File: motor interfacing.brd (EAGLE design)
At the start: 160 x 100 mm, 14 parts

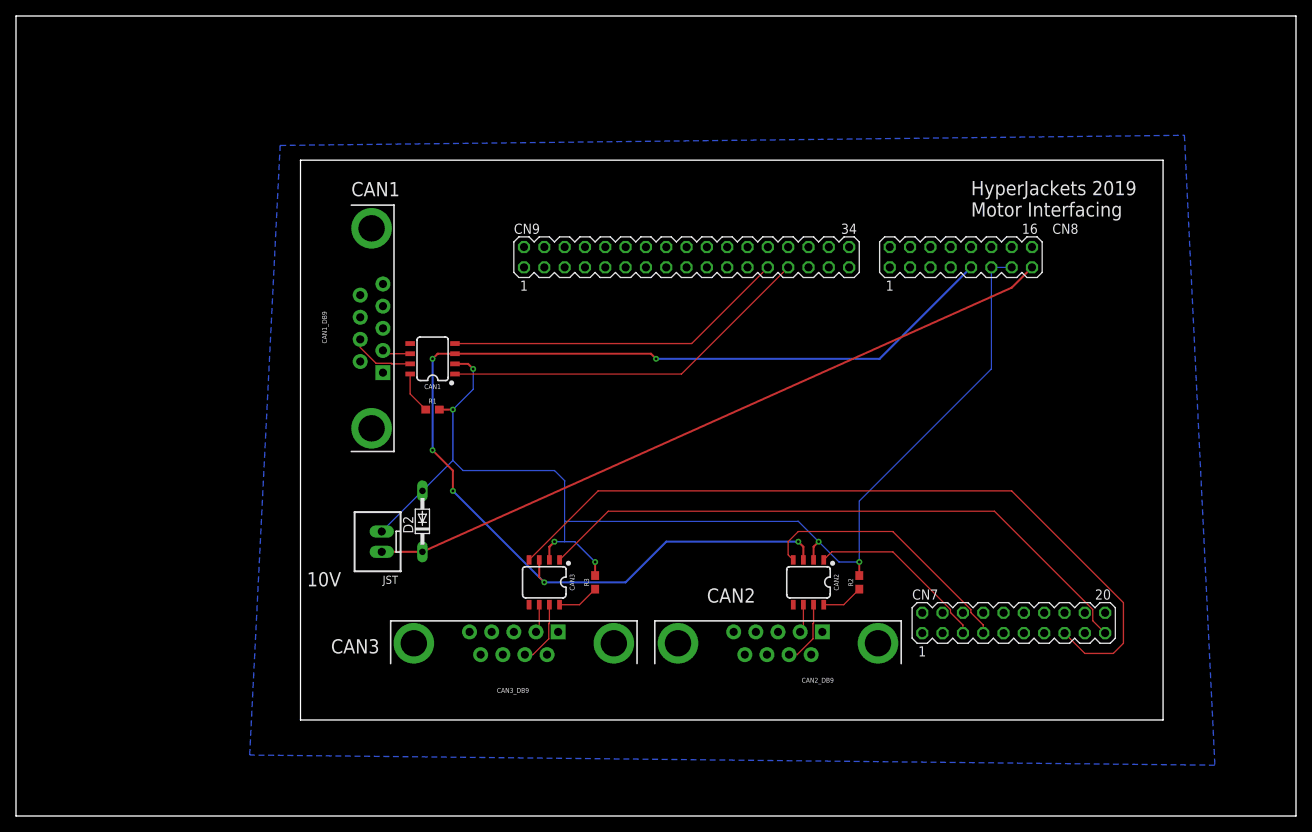
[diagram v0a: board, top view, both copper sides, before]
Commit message: Update motor interfacing board
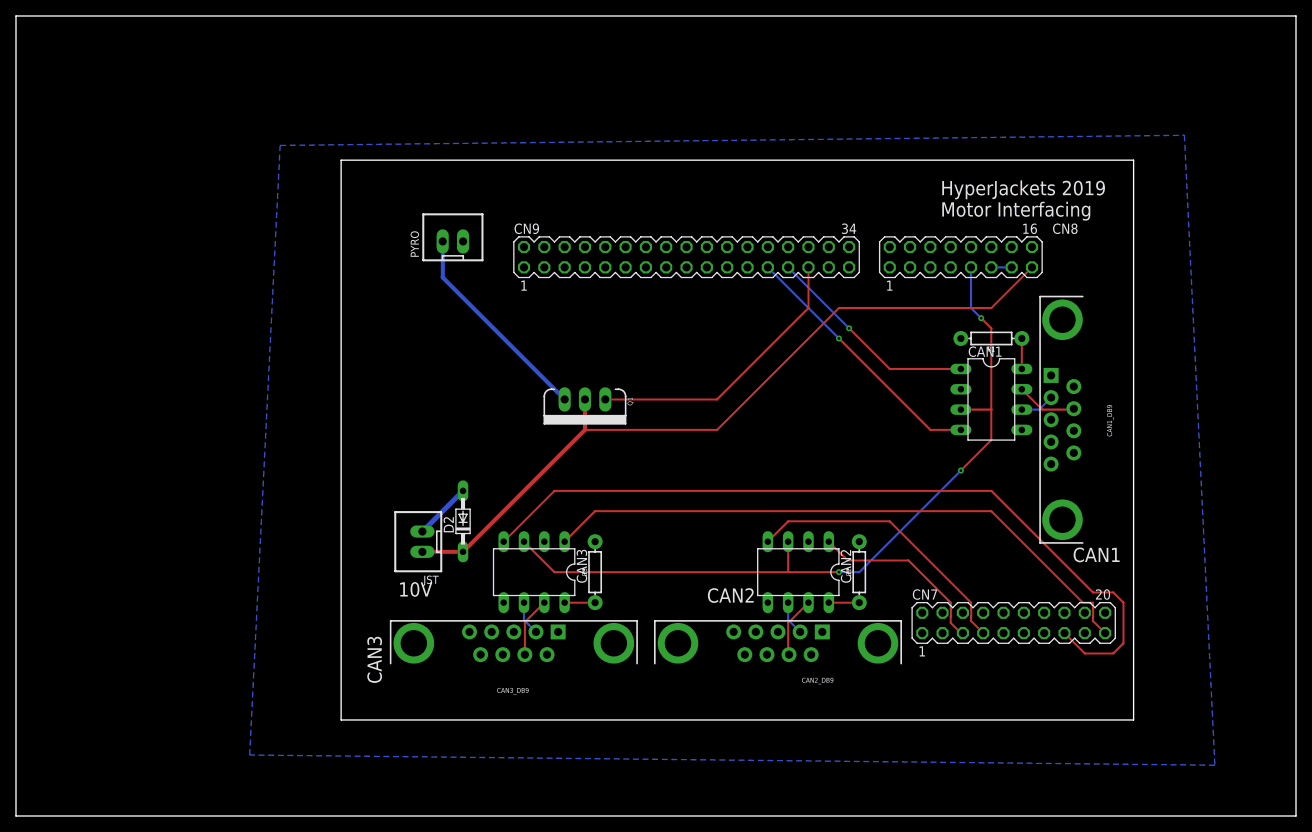
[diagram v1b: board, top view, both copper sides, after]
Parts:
- added PYRO: JST-XH-02-PIN-LONG-PAD, Rembrandt Electronics - JST XH Connectors v1-0:JST-XH-02-PACKAGE-LONG-PAD
- added Q1: 60V/32A/35mΩ, SparkFun-DiscreteSemi:TO220V
- CAN1, CAN2, CAN3: device SparkFun-IC-Comms:SO08 -> elm:MPC2551
- R1, R2, R3: device SparkFun-Resistors:0603 -> SparkFun-Resistors:AXIAL-0.3
- moved CAN1_DB9 87.1 mm to (130.8, 49.5), turned to 270 degrees
- moved R1 70.4 mm to (121.9, 59.7), turned to 180 degrees
- moved CAN1 64.9 mm to (116.8, 53.3), turned to 270 degrees
- moved CAN2 6.35 mm to (99.1, 35.6)
- moved CAN3 6.35 mm to (66.0, 35.6)
- moved D2 5.08 mm to (55.9, 36.8)
- moved JST 5.08 mm to (50.8, 34.3)
- moved R2 1.27 mm to (105.4, 30.5)
- moved R3 1.27 mm to (72.4, 30.5)
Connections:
- new net N$10: PYRO.1, Q1.3
- new net PG0: CN9.29, Q1.1
- net GND: now also PYRO.2, R1.P$2, R2.P$2, R3.P$2; no longer R1.2, R2.2, R3.2
- net N$7: now also R1.P$1; no longer R1.1
- net N$8: now also R2.P$1; no longer R2.1
- net N$9: now also R3.P$1; no longer R3.1
- net VCC: now also Q1.2
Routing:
- net GND: track 151.7 -> 9.72 mm, vias 6 -> 0
- net 5V: track 145.8 -> 97.1 mm, vias 6 -> 3
- net PG0: track 0.00 -> 35.2 mm
- net N$10: track 0.00 -> 26.1 mm
- net PD1: track 47.2 -> 26.9 mm, vias 0 -> 1
- net PD0: track 43.1 -> 32.5 mm, vias 0 -> 1
- net VCC: track 89.4 -> 94.7 mm
- net PB3: track 97.7 -> 99.9 mm
- net PB12: track 33.5 -> 35.1 mm
- net N$9: track 5.25 -> 3.81 mm
- net N$7: track 5.25 -> 3.81 mm
- net N$8: track 5.25 -> 3.81 mm
- net PB4: track 77.9 -> 76.8 mm
- net N$4: track 3.57 -> 4.28 mm
- net N$3: track 3.57 -> 4.28 mm
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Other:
- outline, holes or cut-outs redrawn
